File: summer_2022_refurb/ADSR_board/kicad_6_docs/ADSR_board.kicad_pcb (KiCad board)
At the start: 2 copper layers, 172.7 x 107.9 mm, 124 parts, among them J1 ribbon_port, J2 modosc_port, J3 VCO_port, J4 VCF_port, J5 power_entry, Q201 2N7002, Q202 MMBT3904, Q203 MMBT3904, Q204 MMBT3904, Q301 2N7002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

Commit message: Change directory structure, minor schem and pcb tweaks
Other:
- board text added: "ADSR board rev 0 2022-06-16"
- board text removed: "ADSR board rev 0 2022-06-12"
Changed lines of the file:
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@@
   (title_block
     (title "Josh Ox Ribbon Synth ADSR board")
-    (date "2022-06-12")
+    (date "2022-06-16")
     (rev "0")
     (comment 2 "creativecommons.org/licences/by/4.0")
@@
   (net 34 "/VCA_ADSR/GATE")
   (net 35 "Net-(D401-Pad1)")
-  (net 36 "Net-(R102-Pad2)")
-  (net 37 "Net-(R102-Pad1)")
+  (net 36 "Net-(J3-Pad2)")
+  (net 37 "Net-(R101-Pad2)")
   (net 38 "Net-(D403-Pad1)")
   (net 39 "Net-(U101-Pad1)")
@@
     (property "Sheetfile" "ADSR_board.kicad_sch")
     (property "Sheetname" "")
-    (attr through_hole)
+    (property "exclude_from_bom" "")
+    (attr through_hole exclude_from_bom)
     (fp_text reference "TP3" (at 0 2.5) (layer "B.SilkS")
       (effects (font (size 1 1) (thickness 0.15)) (justify mirror))
@@
     (property "Sheetfile" "power_supply.kicad_sch")
     (property "Sheetname" "power_supply")
-    (attr through_hole)
+    (property "exclude_from_bom" "")
+    (attr through_hole exclude_from_bom)
     (fp_text reference "TP502" (at -2.54 0 -180) (layer "B.SilkS")
       (effects (font (size 1 1) (thickness 0.15)) (justify mirror))
@@
     (property "Sheetfile" "ADSR_board.kicad_sch")
     (property "Sheetname" "")
-    (attr through_hole)
+    (property "exclude_from_bom" "")
+    (attr through_hole exclude_from_bom)
     (fp_text reference "TP1" (at 0 2.5) (layer "B.SilkS")
       (effects (font (size 1 1) (thickness 0.15)) (justify mirror))
@@
     (property "Sheetfile" "ADSR_board.kicad_sch")
     (property "Sheetname" "")
-    (attr through_hole)
+    (property "exclude_from_bom" "")
+    (attr through_hole exclude_from_bom)
     (fp_text reference "TP7" (at 0 2.5) (layer "B.SilkS")
       (effects (font (size 1 1) (thickness 0.15)) (justify mirror))
@@
     (property "Sheetfile" "ADSR_board.kicad_sch")
     (property "Sheetname" "")
-    (attr through_hole)
+    (property "exclude_from_bom" "")
+    (attr through_hole exclude_from_bom)
     (fp_text reference "TP5" (at 0 2.5) (layer "B.SilkS")
       (effects (font (size 1 1) (thickness 0.15)) (justify mirror))
@@
     (fp_circle (center 0 0) (end 1.25 0) (layer "B.Fab") (width 0.15) (fill none))
     (pad "1" thru_hole circle (at 0 0 180) (size 2 2) (drill 1) (layers *.Cu *.Mask)
-      (net 36 "Net-(R102-Pad2)") (pinfunction "1") (pintype "passive"))
+      (net 36 "Net-(J3-Pad2)") (pinfunction "1") (pintype "passive"))
     (model "${KICAD6_3DMODEL_DIR}/TestPoint.3dshapes/TestPoint_Keystone_5000-5004_Miniature.wrl"
       (offset (xyz 0 0 0))
@@
     (fp_line (start -1 -0.625) (end -1 0.625) (layer "B.Fab") (width 0.1))
     (pad "1" smd roundrect (at -0.9125 0 180) (size 1.025 1.4) (layers "B.Cu" "B.Paste" "B.Mask") (roundrect_rratio 0.243902)
-      (net 37 "Net-(R102-Pad1)") (pintype "passive"))
+      (net 37 "Net-(R101-Pad2)") (pintype "passive"))
     (pad "2" smd roundrect (at 0.9125 0 180) (size 1.025 1.4) (layers "B.Cu" "B.Paste" "B.Mask") (roundrect_rratio 0.243902)
-      (net 36 "Net-(R102-Pad2)") (pintype "passive"))
+      (net 36 "Net-(J3-Pad2)") (pintype "passive"))
     (model "${KICAD6_3DMODEL_DIR}/Resistor_SMD.3dshapes/R_0805_2012Metric.wrl"
       (offset (xyz 0 0 0))
@@
     (property "Sheetfile" "ADSR_board.kicad_sch")
     (property "Sheetname" "")
-    (attr through_hole)
+    (property "exclude_from_bom" "")
+    (attr through_hole exclude_from_bom)
     (fp_text reference "TP2" (at 0 2.5) (layer "B.SilkS")
       (effects (font (size 1 1) (thickness 0.15)) (justify mirror))
@@
     (property "Sheetfile" "ADSR_board.kicad_sch")
     (property "Sheetname" "")
-    (attr through_hole)
+    (property "exclude_from_bom" "")
+    (attr through_hole exclude_from_bom)
     (fp_text reference "TP4" (at 0 2.5) (layer "B.SilkS")
       (effects (font (size 1 1) (thickness 0.15)) (justify mirror))
@@
     (property "Sheetfile" "power_supply.kicad_sch")
     (property "Sheetname" "power_supply")
-    (attr through_hole)
+    (property "exclude_from_bom" "")
+    (attr through_hole exclude_from_bom)
     (fp_text reference "TP501" (at 0 2.5) (layer "B.SilkS")
       (effects (font (size 1 1) (thickness 0.15)) (justify mirror))
@@
       (net 3 "/modulation_ADSR/OUT") (pinfunction "Pin_1") (pintype "passive"))
     (pad "2" thru_hole oval (at 2.54 0 270) (size 1.74 2.19) (drill 1.19) (layers *.Cu *.Mask)
-      (net 36 "Net-(R102-Pad2)") (pinfunction "Pin_2") (pintype "passive"))
+      (net 36 "Net-(J3-Pad2)") (pinfunction "Pin_2") (pintype "passive"))
     (pad "3" thru_hole oval (at 5.08 0 270) (size 1.74 2.19) (drill 1.19) (layers *.Cu *.Mask)
       (net 23 "GND") (pinfunction "Pin_3") (pintype "passive"))
@@
     (property "Sheetfile" "power_supply.kicad_sch")
     (property "Sheetname" "power_supply")
-    (attr through_hole)
+    (property "exclude_from_bom" "")
+    (attr through_hole exclude_from_bom)
     (fp_text reference "TP503" (at 0 2.5) (layer "B.SilkS")
       (effects (font (size 1 1) (thickness 0.15)) (justify mirror))
@@
     (property "Sheetfile" "ADSR_board.kicad_sch")
     (property "Sheetname" "")
-    (attr through_hole)
+    (property "exclude_from_bom" "")
+    (attr through_hole exclude_from_bom)
     (fp_text reference "TP6" (at 0 2.5) (layer "B.SilkS")
       (effects (font (size 1 1) (thickness 0.15)) (justify mirror))
@@
       (net 23 "GND") (pinfunction "+") (pintype "input"))
     (pad "6" smd roundrect (at 3.5 -0.635 180) (size 1.9 0.6) (layers "B.Cu" "B.Paste" "B.Mask") (roundrect_rratio 0.25)
-      (net 37 "Net-(R102-Pad1)") (pinfunction "-") (pintype "input"))
+      (net 37 "Net-(R101-Pad2)") (pinfunction "-") (pintype "input"))
     (pad "7" smd roundrect (at 3.5 0.635 180) (size 1.9 0.6) (layers "B.Cu" "B.Paste" "B.Mask") (roundrect_rratio 0.25)
-      (net 36 "Net-(R102-Pad2)") (pintype "output"))
+      (net 36 "Net-(J3-Pad2)") (pintype "output"))
     (pad "8" smd roundrect (at 3.5 1.905 180) (size 1.9 0.6) (layers "B.Cu" "B.Paste" "B.Mask") (roundrect_rratio 0.25)
       (net 22 "+15V") (pinfunction "V+") (pintype "power_in"))
@@
       (net 3 "/modulation_ADSR/OUT") (pintype "passive"))
     (pad "2" smd roundrect (at 0.9125 0) (size 1.025 1.4) (layers "B.Cu" "B.Paste" "B.Mask") (roundrect_rratio 0.243902)
-      (net 37 "Net-(R102-Pad1)") (pintype "passive"))
+      (net 37 "Net-(R101-Pad2)") (pintype "passive"))
     (model "${KICAD6_3DMODEL_DIR}/Resistor_SMD.3dshapes/R_0805_2012Metric.wrl"
       (offset (xyz 0 0 0))
@@
     (effects (font (size 1 1) (thickness 0.15)) (justify mirror))
   )
-  (gr_text "ADSR board\nrev 0\n2022-06-12" (at 76.2 52.832) (layer "B.SilkS")
+  (gr_text "ADSR board\nrev 0\n2022-06-16" (at 76.2 52.832) (layer "B.SilkS")
     (effects (font (size 1 1) (thickness 0.15)) (justify left mirror))
   )

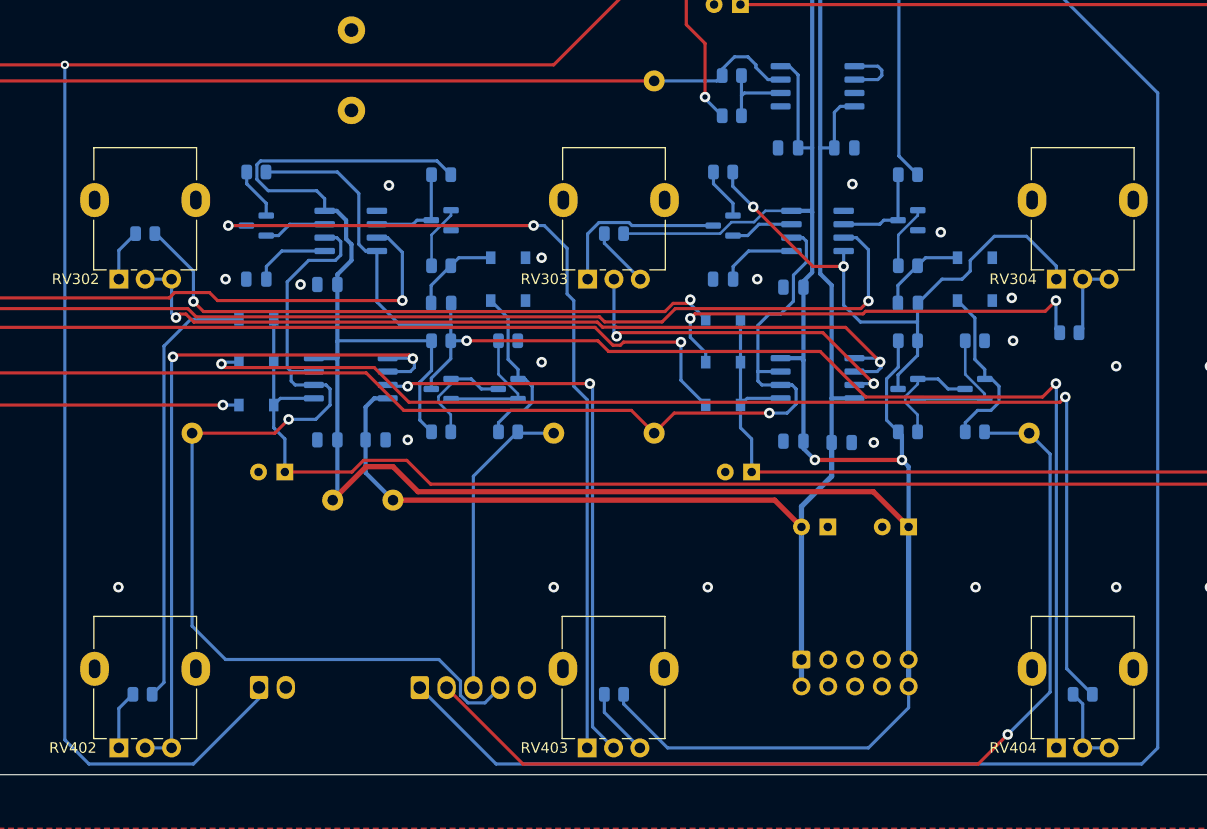
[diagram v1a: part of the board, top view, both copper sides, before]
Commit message: Add cool kibuzzard labels, minor tweaks
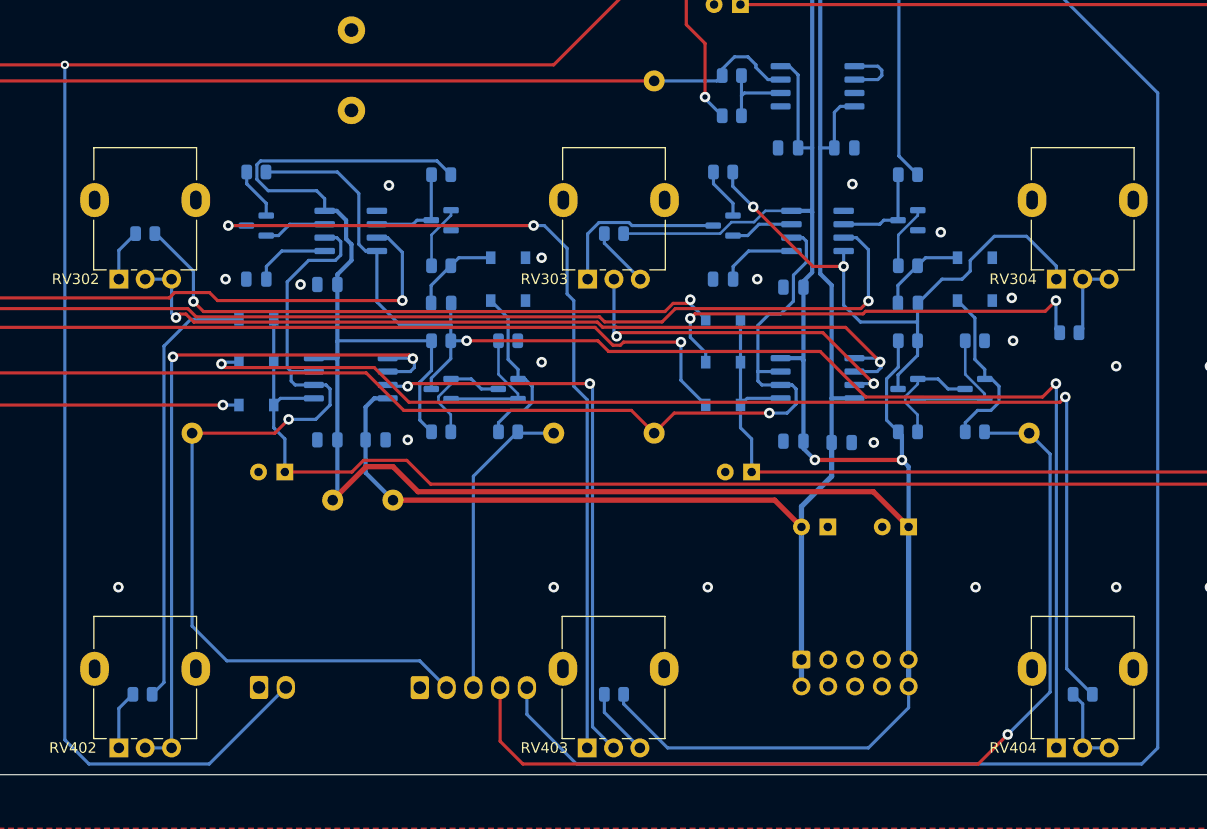
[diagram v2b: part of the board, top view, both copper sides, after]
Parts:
- added REF**: OSHW-Logo_5.7x6mm_SilkScreen, Symbol:OSHW-Logo_5.7x6mm_SilkScreen, B.Cu at (64.3, 53.3)
- added kibuzzard-62AC755C: G***, kibuzzard-62AC755C, B.Cu at (139.7, 107.3)
- added kibuzzard-62AC755C: G***, kibuzzard-62AC755C, B.Cu at (34.2, 62.2)
- added kibuzzard-62AC755C: G***, kibuzzard-62AC755C, B.Cu at (34.2, 106.7)
- added kibuzzard-62AC755C: G***, kibuzzard-62AC755C, B.Cu at (91.9, 64.5)
- added kibuzzard-62AC755C: G***, kibuzzard-62AC755C, B.Cu at (98.4, 109.9)
- added kibuzzard-62AC755C: G***, kibuzzard-62AC755C, B.Cu at (83.2, 109.9)
- added kibuzzard-62AC758B: G***, kibuzzard-62AC758B, B.Cu at (35.2, 57.1)
- added kibuzzard-62AC7596: G***, kibuzzard-62AC7596, B.Cu at (36.7, 59.7)
- added kibuzzard-62AC762D: G***, kibuzzard-62AC762D, B.Cu at (35.2, 104.1)
- added kibuzzard-62AC769B: G***, kibuzzard-62AC769B, B.Cu at (85.7, 109.0)
- added kibuzzard-62AC7711: G***, kibuzzard-62AC7711, B.Cu at (108.6, 107.0)
- added kibuzzard-62AC7737: G***, kibuzzard-62AC7737, B.Cu at (106.0, 107.0)
- added kibuzzard-62AC7758: G***, kibuzzard-62AC7758, B.Cu at (103.5, 107.0)
- added kibuzzard-62AC7771: G***, kibuzzard-62AC7771, B.Cu at (101.0, 109.0)
- added kibuzzard-62AC77C9: G***, kibuzzard-62AC77C9, B.Cu at (22.2, 59.7)
- added kibuzzard-62AC77E4: G***, kibuzzard-62AC77E4, B.Cu at (22.2, 105.4)
- added kibuzzard-62AC77FB: G***, kibuzzard-62AC77FB, B.Cu at (103.5, 121.9)
- added kibuzzard-62AC7810: G***, kibuzzard-62AC7810, B.Cu at (84.5, 121.9)
- added kibuzzard-62AC78CB: G***, kibuzzard-62AC78CB, B.Cu at (139.7, 121.9)
- added kibuzzard-62AC791A: G***, kibuzzard-62AC791A, B.Cu at (90.2, 101.6)
- added kibuzzard-62AC791A: G***, kibuzzard-62AC791A, B.Cu at (144.8, 107.3)
- added kibuzzard-62AC792A: G***, kibuzzard-62AC792A, B.Cu at (134.6, 107.3)
- added kibuzzard-62AC792A: G***, kibuzzard-62AC792A, B.Cu at (100.3, 98.4)
- added kibuzzard-62AC795F: G***, kibuzzard-62AC795F, B.Cu at (156.2, 50.8)
- added kibuzzard-62AC7972: G***, kibuzzard-62AC7972, B.Cu at (119.4, 50.8)
- added kibuzzard-62AC7989: G***, kibuzzard-62AC7989, B.Cu at (119.4, 61.6)
- added kibuzzard-62AC79A3: G***, kibuzzard-62AC79A3, B.Cu at (76.2, 95.2)
- added kibuzzard-62AC79B4: G***, kibuzzard-62AC79B4, B.Cu at (109.2, 95.2)
- added kibuzzard-62AC79C5: G***, kibuzzard-62AC79C5, B.Cu at (120.7, 95.2)
- added kibuzzard-62AC79E0: G***, kibuzzard-62AC79E0, B.Cu at (156.2, 95.2)
- added kibuzzard-62AC7A9F: G***, kibuzzard-62AC7A9F, B.Cu at (61.6, 47.6)
- added kibuzzard-62AC7ABD: G***, kibuzzard-62AC7ABD, B.Cu at (72.4, 53.3)
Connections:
- J1 pad 1: /modulation_ADSR/GATE -> GND
- J1 pad 2: /VCF_ADSR/GATE -> /VCA_ENV
- J1 pad 4: /VCA_ENV -> /VCF_ADSR/GATE
- J1 pad 5: GND -> /modulation_ADSR/GATE
- J2 pad 1: /modulation_ADSR/OUT -> GND
- J2 pad 2: GND -> /modulation_ADSR/OUT
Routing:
- net /modulation_ADSR/GATE: track 157.1 -> 148.5 mm
- net /VCA_ENV: track 92.4 -> 85.3 mm
- net /VCF_ADSR/GATE: track 92.7 -> 90.6 mm
- net /modulation_ADSR/OUT: track 236.3 -> 238.2 mm
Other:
- board text removed: "ADSR board rev 0 2022-06-16"
- board text removed: "DC POWER IN"
- board text removed: "GND"
- board text removed: "INV MOD ENV O"
- board text removed: "MOD ENV I"
- board text removed: "MOD ENV O"
- board text removed: "MODOSC BOARD PORT"
- board text removed: "Ox Ribbon Synth"
- board text removed: "RIBBON BOARD PORT"
- board text removed: "V+"
- board text removed: "V-"
- board text removed: "VCA ENV I"
- board text removed: "VCA ENV O"
- board text removed: "VCA env"
- board text removed: "VCA env gate"
- board text removed: "VCF BOARD PORT"
- board text removed: "VCF ENV I"
- board text removed: "VCF ENV O"
- board text removed: "VCF env"
- board text removed: "VCF env gate"
- board text removed: "VCO BOARD PORT"
- board text removed: "inv mod env"
- board text removed: "mod env"
- board text removed: "mod env gate"
